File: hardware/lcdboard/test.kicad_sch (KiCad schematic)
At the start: 23 parts, among them J1 Conn_01x11_Female, J2 Conn_01x08_Shielded, J3 Conn_01x45, J4 Conn_01x11_Female, U1 AP2502

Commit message: restructure, adding branch for mux'd display board
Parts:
- added U2: 74LS157, Package_SO:TSSOP-16_4.4x5mm_P0.65mm, symbol 74xx:74LS157
- renumbered C2 to C1, C3 to C2, C4 to C3, J3 to J1, J4 to J3, J1 to J4, R11 to R1, R3 to R10, R7 to R11, R1 to R2, R2 to R3, R9 to R4, R4 to R5, R8 to R7, R10 to R8, R5 to R9, RN3 to RN1, RN4 to RN3, RN1 to RN4

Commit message: added 74CBLTV3257
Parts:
- removed RN2, RN4: 100k, Resistor_SMD:R_Array_Concave_4x0402, symbol Device:R_Pack04
- removed U2: 74LS157, Package_SO:TSSOP-16_4.4x5mm_P0.65mm, symbol 74xx:74LS157
- added RN? (x2): 100k, Resistor_SMD:R_Array_Concave_4x0402, symbol Device:R_Pack04
- added U? (x5): 74CBTLV3257, symbol 74xx:74CBTLV3257
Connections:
- net CS: no longer J4.11 (Pin_11), R8.1
- net DE: no longer J3.4 (Pin_4)
- net GND: now also RN?.5 (R4.2), RN?.6 (R3.2), RN?.7 (R2.2), RN?.8 (R1.2)
- net HSYNC: no longer J3.2 (Pin_2)
- net MISO: no longer J4.7 (Pin_7)
- net MOSI: no longer J4.8 (Pin_8)
- net PCLK: no longer J3.3 (Pin_3)
- net RS: no longer J4.10 (Pin_10)
- net SCLK: no longer J4.9 (Pin_9)
- net VSYNC: no longer J3.1 (Pin_1)
- new net: J4.11 (Pin_11), R8.1
- new net: RN?.5 (R4.2), RN?.6 (R3.2), RN?.7 (R2.2), RN?.8 (R1.2)

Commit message: schematic complete unreviewed
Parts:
- removed U? (x5): 74CBTLV3257, symbol 74xx:74CBTLV3257
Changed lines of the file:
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@@
     (pin "9")
   )
-  (symbol (lib_id "74xx:74CBTLV3257") (at 123.19 96.52 0) (unit 2)
-    (in_bom yes) (on_board yes) (fields_autoplaced)
-    (property "Reference" "U?" (id 0) (at 123.19 86.36 0))
-    (property "Value" "74CBTLV3257" (id 1) (at 123.19 88.9 0))
-    (property "Footprint" "" (id 2) (at 121.92 96.52 0)
-      (effects (font (size 1.27 1.27)) hide)
-    )
-    (property "Datasheet" "http://www.ti.com/lit/ds/symlink/sn74cbtlv3257.pdf" (id 3) (at 121.92 96.52 0)
-      (effects (font (size 1.27 1.27)) hide)
-    )
-    (pin "2")
-    (pin "3")
-    (pin "4")
-    (pin "5")
-    (pin "6")
-    (pin "7")
-    (pin "10")
-    (pin "11")
-    (pin "9")
-    (pin "12")
-    (pin "13")
-    (pin "14")
-    (pin "1")
-    (pin "15")
-    (pin "16")
-    (pin "8")
-  )
   (symbol (lib_id "power:+3V3") (at 224.79 36.83 0) (unit 1)
     (in_bom yes) (on_board yes)
@@
     )
     (pin "1")
-  )
-  (symbol (lib_id "74xx:74CBTLV3257") (at 143.51 95.25 0) (unit 3)
-    (in_bom yes) (on_board yes) (fields_autoplaced)
-    (property "Reference" "U?" (id 0) (at 143.51 85.09 0))
-    (property "Value" "74CBTLV3257" (id 1) (at 143.51 87.63 0))
-    (property "Footprint" "" (id 2) (at 142.24 95.25 0)
-      (effects (font (size 1.27 1.27)) hide)
-    )
-    (property "Datasheet" "http://www.ti.com/lit/ds/symlink/sn74cbtlv3257.pdf" (id 3) (at 142.24 95.25 0)
-      (effects (font (size 1.27 1.27)) hide)
-    )
-    (pin "2")
-    (pin "3")
-    (pin "4")
-    (pin "5")
-    (pin "6")
-    (pin "7")
-    (pin "10")
-    (pin "11")
-    (pin "9")
-    (pin "12")
-    (pin "13")
-    (pin "14")
-    (pin "1")
-    (pin "15")
-    (pin "16")
-    (pin "8")
-  )
-  (symbol (lib_id "74xx:74CBTLV3257") (at 121.92 114.3 0) (unit 4)
-    (in_bom yes) (on_board yes) (fields_autoplaced)
-    (property "Reference" "U?" (id 0) (at 121.92 104.14 0))
-    (property "Value" "74CBTLV3257" (id 1) (at 121.92 106.68 0))
-    (property "Footprint" "" (id 2) (at 120.65 114.3 0)
-      (effects (font (size 1.27 1.27)) hide)
-    )
-    (property "Datasheet" "http://www.ti.com/lit/ds/symlink/sn74cbtlv3257.pdf" (id 3) (at 120.65 114.3 0)
-      (effects (font (size 1.27 1.27)) hide)
-    )
-    (pin "2")
-    (pin "3")
-    (pin "4")
-    (pin "5")
-    (pin "6")
-    (pin "7")
-    (pin "10")
-    (pin "11")
-    (pin "9")
-    (pin "12")
-    (pin "13")
-    (pin "14")
-    (pin "1")
-    (pin "15")
-    (pin "16")
-    (pin "8")
   )
   (symbol (lib_id "power:GND") (at 147.32 133.35 0) (unit 1)
@@
     (pin "S2")
   )
-  (symbol (lib_id "74xx:74CBTLV3257") (at 156.21 109.22 0) (unit 5)
-    (in_bom yes) (on_board yes) (fields_autoplaced)
-    (property "Reference" "U?" (id 0) (at 161.29 107.9499 0)
-      (effects (font (size 1.27 1.27)) (justify left))
-    )
-    (property "Value" "74CBTLV3257" (id 1) (at 161.29 110.4899 0)
-      (effects (font (size 1.27 1.27)) (justify left))
-    )
-    (property "Footprint" "" (id 2) (at 154.94 109.22 0)
-      (effects (font (size 1.27 1.27)) hide)
-    )
-    (property "Datasheet" "http://www.ti.com/lit/ds/symlink/sn74cbtlv3257.pdf" (id 3) (at 154.94 109.22 0)
-      (effects (font (size 1.27 1.27)) hide)
-    )
-    (pin "2")
-    (pin "3")
-    (pin "4")
-    (pin "5")
-    (pin "6")
-    (pin "7")
-    (pin "10")
-    (pin "11")
-    (pin "9")
-    (pin "12")
-    (pin "13")
-    (pin "14")
-    (pin "1")
-    (pin "15")
-    (pin "16")
-    (pin "8")
-  )
   (symbol (lib_id "power:+3V3") (at 140.97 123.19 0) (unit 1)
     (in_bom yes) (on_board yes)
@@
     )
     (pin "1")
-  )
-  (symbol (lib_id "74xx:74CBTLV3257") (at 123.19 77.47 0) (unit 1)
-    (in_bom yes) (on_board yes) (fields_autoplaced)
-    (property "Reference" "U?" (id 0) (at 123.19 67.31 0))
-    (property "Value" "74CBTLV3257" (id 1) (at 123.19 69.85 0))
-    (property "Footprint" "" (id 2) (at 121.92 77.47 0)
-      (effects (font (size 1.27 1.27)) hide)
-    )
-    (property "Datasheet" "http://www.ti.com/lit/ds/symlink/sn74cbtlv3257.pdf" (id 3) (at 121.92 77.47 0)
-      (effects (font (size 1.27 1.27)) hide)
-    )
-    (pin "2")
-    (pin "3")
-    (pin "4")
-    (pin "5")
-    (pin "6")
-    (pin "7")
-    (pin "10")
-    (pin "11")
-    (pin "9")
-    (pin "12")
-    (pin "13")
-    (pin "14")
-    (pin "1")
-    (pin "15")
-    (pin "16")
-    (pin "8")
   )
   (symbol (lib_id "Device:R_Small") (at 116.84 46.99 180) (unit 1)
@@
       (reference "U1") (unit 1) (value "AP2502") (footprint "Package_TO_SOT_SMD:SOT-23-6")
     )
-    (path "/a162abfb-26f5-4e85-90d4-bb1627c202a7"
-      (reference "U?") (unit 1) (value "74CBTLV3257") (footprint "Package_SO:TSSOP-16_4.4x5mm_P0.65mm")
-    )
-    (path "/4a0105e0-6e23-41fb-90aa-e6380344c42e"
-      (reference "U?") (unit 2) (value "74CBTLV3257") (footprint "Package_SO:TSSOP-16_4.4x5mm_P0.65mm")
-    )
-    (path "/53a37b36-3e0e-4979-b4cb-948efa215072"
-      (reference "U?") (unit 3) (value "74CBTLV3257") (footprint "Package_SO:TSSOP-16_4.4x5mm_P0.65mm")
-    )
-    (path "/5a3a8ab8-1f8a-4d95-bee8-6ef02c652fa3"
-      (reference "U?") (unit 4) (value "74CBTLV3257") (footprint "Package_SO:TSSOP-16_4.4x5mm_P0.65mm")
-    )
-    (path "/906e02e9-212a-48d2-b32e-b5600a0663c8"
-      (reference "U?") (unit 5) (value "74CBTLV3257") (footprint "Package_SO:TSSOP-16_4.4x5mm_P0.65mm")
-    )
-  )
+  )

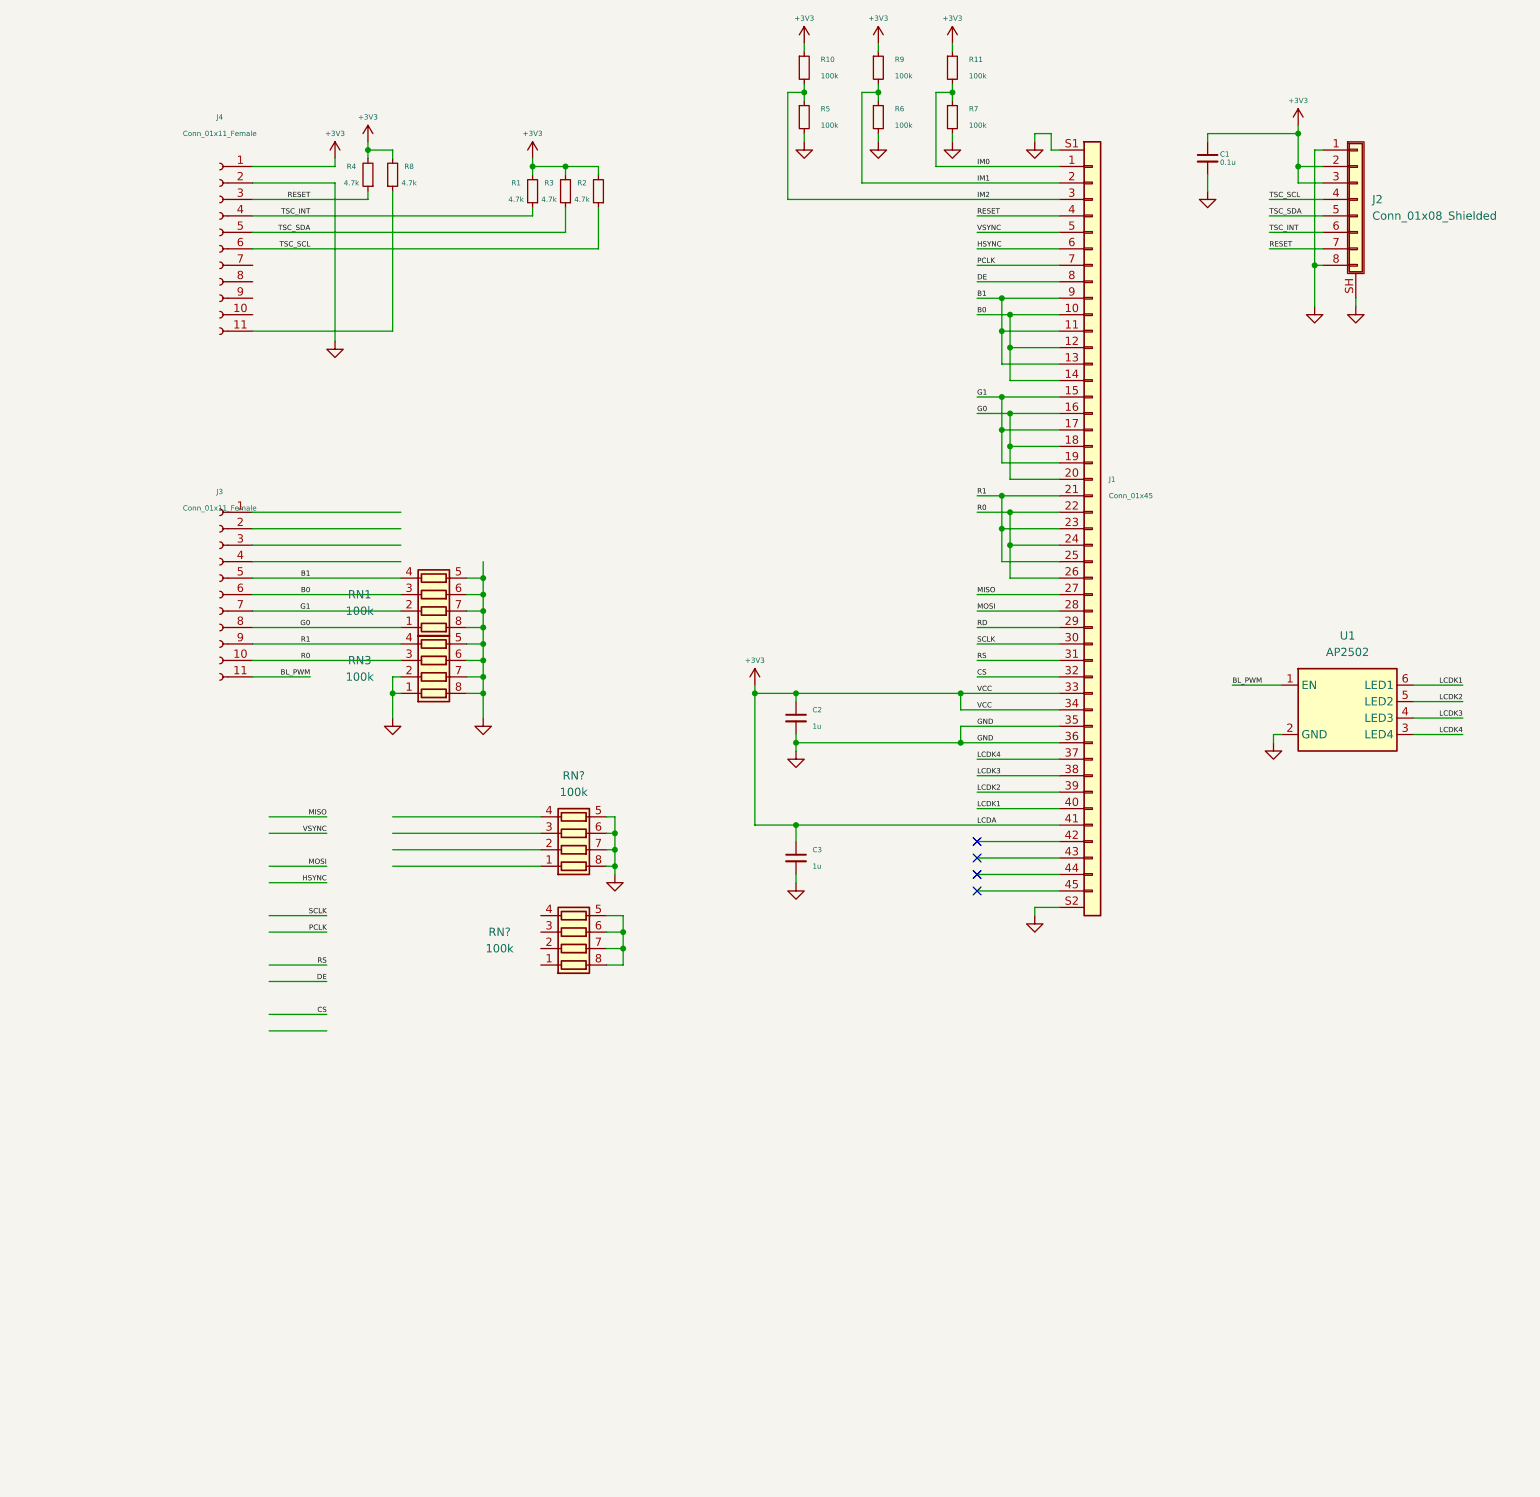
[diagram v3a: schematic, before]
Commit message: split back out condensed board into lcdboard and base
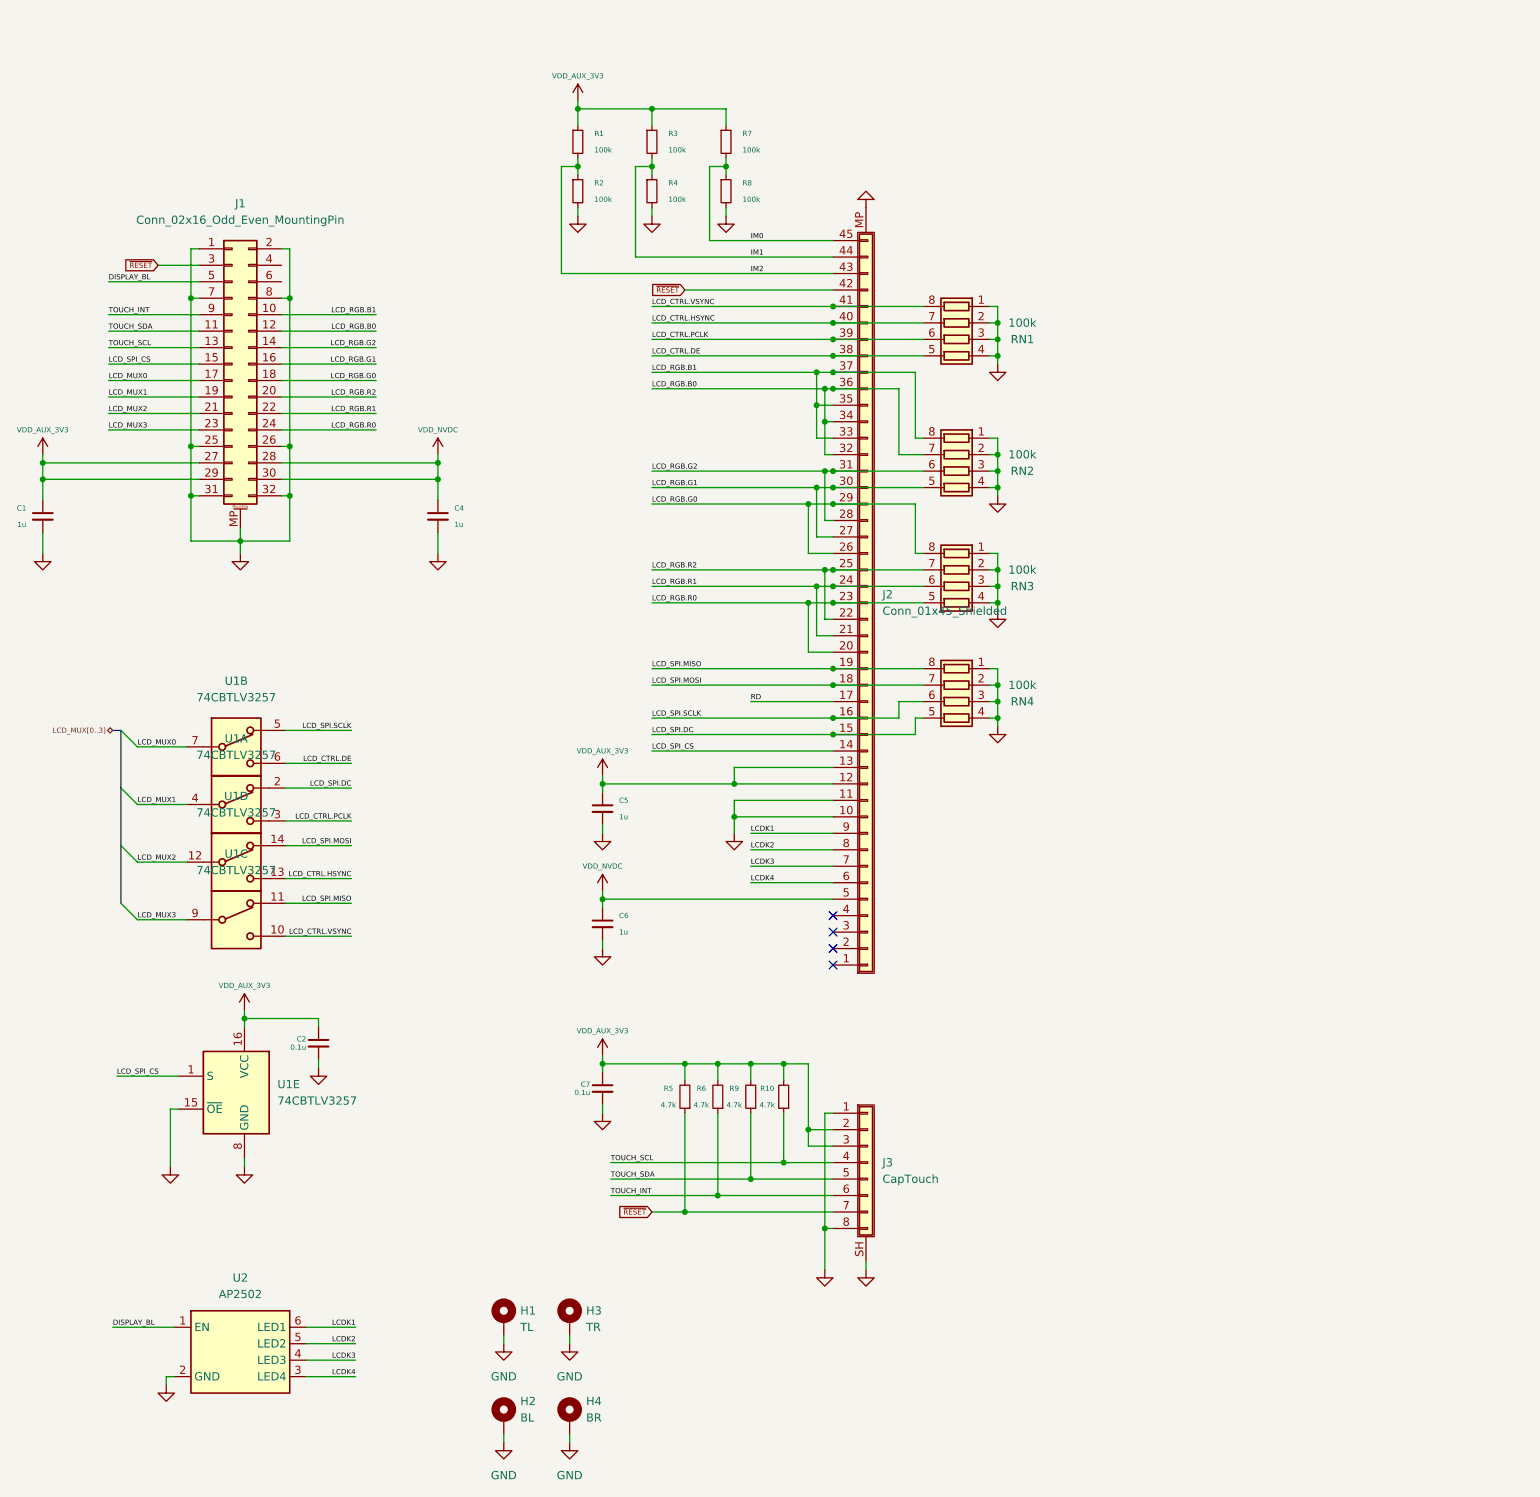
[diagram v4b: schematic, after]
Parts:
- removed C3: 1u, Capacitor_SMD:C_0603_1608Metric, symbol Device:C_Small
- removed J1: Conn_01x45, Connector_FFC-FPC:Hirose_FH12-45S-0.5SH_1x45-1MP_P0.50mm_Horizontal, symbol Connector_Generic:Conn_01x40
- removed J2: Conn_01x08_Shielded, Connector_FFC-FPC:TE_0-1734839-8_1x08-1MP_P0.5mm_Horizontal, symbol Connector_Generic_Shielded:Conn_01x08_Shielded
- removed J3, J4: Conn_01x11_Female, Connector_PinHeader_2.54mm:PinHeader_1x11_P2.54mm_Vertical, symbol Connector:Conn_01x11_Female
- removed R11: 100k, Resistor_SMD:R_0402_1005Metric, symbol Device:R_Small
- removed RN? (x2): 100k, Resistor_SMD:R_Array_Concave_4x0402, symbol Device:R_Pack04
- removed U1: AP2502, Package_TO_SOT_SMD:SOT-23-6, symbol bt_PMIC_Linear:AP2502
- added C4, C5, C6: 1u, Capacitor_SMD:C_0603_1608Metric, symbol Device:C_Small
- added C7: 0.1u, Capacitor_SMD:C_0402_1005Metric, symbol Device:C_Small
- added H1: TL, Mounting_Wuerth:Mounting_Wuerth_WA-SMSI-M1.6_H2mm_9774020633, symbol Mechanical:MountingHole_Pad
- added H2: BL, Mounting_Wuerth:Mounting_Wuerth_WA-SMSI-M1.6_H2mm_9774020633, symbol Mechanical:MountingHole_Pad
- added H3: TR, Mounting_Wuerth:Mounting_Wuerth_WA-SMSI-M1.6_H2mm_9774020633, symbol Mechanical:MountingHole_Pad
- added H4: BR, Mounting_Wuerth:Mounting_Wuerth_WA-SMSI-M1.6_H2mm_9774020633, symbol Mechanical:MountingHole_Pad
- added J1: Conn_02x16_Odd_Even_MountingPin, Connector_Molex:Molex_SlimStack_502426-3210_2x16_P0.40mm_Vertical, symbol Connector_Generic_MountingPin:Conn_02x16_Odd_Even_MountingPin
- added J2: Conn_01x45_Shielded, Connector_FFC-FPC:Hirose_FH12-45S-0.5SH_1x45-1MP_P0.50mm_Horizontal, symbol bt_Connector:Conn_01x45_Shielded
- added J3: CapTouch, Connector_FFC-FPC:TE_0-1734839-8_1x08-1MP_P0.5mm_Horizontal, symbol Connector_Generic_Shielded:Conn_01x08_Shielded
- added RN2, RN4: 100k, Resistor_SMD:R_Array_Concave_4x0402, symbol Device:R_Pack04
- added U1: 74CBTLV3257, Package_SO:TSSOP-16_4.4x5mm_P0.65mm, symbol 74xx:74CBTLV3257
- added U2: AP2502, Package_TO_SOT_SMD:SOT-23-6, symbol bt_PMIC_Linear:AP2502
- C1: value 0.1u -> 1u; footprint Capacitor_SMD:C_0402_1005Metric -> Capacitor_SMD:C_0603_1608Metric
- C2: value 1u -> 0.1u; footprint Capacitor_SMD:C_0603_1608Metric -> Capacitor_SMD:C_0402_1005Metric
- R1, R2, R3, R4, R8: value 4.7k -> 100k
- R10, R5, R6, R9: value 100k -> 4.7k
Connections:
- net B0 is gone; now on net GND: RN1.3 (R3.1)
- net B1 is gone; now on net GND: RN1.4 (R4.1)
- net G0 is gone; now on net GND: RN1.1 (R1.1)
- net G1 is gone; now on net GND: RN1.2 (R2.1)
- net R0 is gone; now on net GND: RN3.3 (R3.1)
- net R1 is gone; now on net GND: RN3.4 (R4.1)
- net RESET is gone; now on net IM1: R4.1
- net TSC_SCL is gone; now on net IM2: R2.1
- net TSC_SDA is gone; now on net VDD_AUX_3V3: R3.1
- net GND: now also R2.2, R4.2, R8.2, C4.2, C5.2, C6.2, C7.2, H1.1, H2.1, H3.1, H4.1, J1.1 (Pin_1), J1.2 (Pin_2), J1.25 (Pin_25), J1.26 (Pin_26), J1.31 (Pin_31), J1.32 (Pin_32), J1.7 (Pin_7), J1.8 (Pin_8), J1.MP (MountPin), J2.10 (Pin_10), J2.11 (Pin_11), J2.MP (Mount), J3.1 (Pin_1), J3.8 (Pin_8), J3.SH (Shield), RN2.1 (R1.1), RN2.2 (R2.1), RN2.3 (R3.1), RN2.4 (R4.1), RN4.1 (R1.1), RN4.2 (R2.1), RN4.3 (R3.1), RN4.4 (R4.1), U1.15 (~{OE}), U1.8 (GND), U2.2 (GND); no longer R5.2, R6.2, R7.2, RN1.5 (R4.2), RN1.6 (R3.2), RN1.7 (R2.2), RN1.8 (R1.2), RN3.5 (R4.2), RN3.6 (R3.2), RN3.7 (R2.2), RN3.8 (R1.2)
- net IM0: now also R7.2, R8.1, J2.45 (Pin_45); no longer R7.1
- net IM1: now also R3.2, J2.44 (Pin_44); no longer R6.1, R9.2
- net IM2: now also R1.2, J2.43 (Pin_43); no longer R10.2, R5.1
- net LCDK1: now also J2.9 (Pin_9), U2.6 (LED1)
- net LCDK2: now also J2.8 (Pin_8), U2.5 (LED2)
- net LCDK3: now also J2.7 (Pin_7), U2.4 (LED3)
- net LCDK4: now also J2.6 (Pin_6), U2.3 (LED4)
- net RD: now also J2.17 (Pin_17)
- removed net +3V3: C1.1, C2.1, R1.2, R10.1, R2.2, R3.2, R4.2, R8.2, R9.1
- net TSC_INT renamed VDD_AUX_3V3
- net VDD_AUX_3V3: now also C1.1, C2.1, R10.2, R5.2, R6.2, R7.1, R9.2, C5.1, C7.1, J1.27 (Pin_27), J1.29 (Pin_29), J2.12 (Pin_12), J2.13 (Pin_13), J3.2 (Pin_2), J3.3 (Pin_3), U1.16 (VCC)
- new net DISPLAY_BL: J1.5 (Pin_5), U2.1 (EN)
- new net LCD_CTRL.DE: J2.38 (Pin_38), RN1.5 (R4.2), U1.6
- new net LCD_CTRL.HSYNC: J2.40 (Pin_40), RN1.7 (R2.2), U1.13
- new net LCD_CTRL.PCLK: J2.39 (Pin_39), RN1.6 (R3.2), U1.3
- new net LCD_CTRL.VSYNC: J2.41 (Pin_41), RN1.8 (R1.2), U1.10
- new net LCD_MUX0: J1.17 (Pin_17), U1.7
- new net LCD_MUX1: J1.19 (Pin_19), U1.4
- new net LCD_MUX2: J1.21 (Pin_21), U1.12
- new net LCD_MUX3: J1.23 (Pin_23), U1.9
- new net LCD_RGB.B0: J1.12 (Pin_12), J2.32 (Pin_32), J2.34 (Pin_34), J2.36 (Pin_36), RN2.7 (R2.2)
- new net LCD_RGB.B1: J1.10 (Pin_10), J2.33 (Pin_33), J2.35 (Pin_35), J2.37 (Pin_37), RN2.8 (R1.2)
- new net LCD_RGB.G0: J1.18 (Pin_18), J2.26 (Pin_26), J2.29 (Pin_29), RN3.8 (R1.2)
- new net LCD_RGB.G1: J1.16 (Pin_16), J2.27 (Pin_27), J2.30 (Pin_30), RN2.5 (R4.2)
- new net LCD_RGB.G2: J1.14 (Pin_14), J2.28 (Pin_28), J2.31 (Pin_31), RN2.6 (R3.2)
- new net LCD_RGB.R0: J1.24 (Pin_24), J2.20 (Pin_20), J2.23 (Pin_23), RN3.5 (R4.2)
- new net LCD_RGB.R1: J1.22 (Pin_22), J2.21 (Pin_21), J2.24 (Pin_24), RN3.6 (R3.2)
- new net LCD_RGB.R2: J1.20 (Pin_20), J2.22 (Pin_22), J2.25 (Pin_25), RN3.7 (R2.2)
- new net LCD_SPI.DC: J2.15 (Pin_15), RN4.5 (R4.2), U1.2
- new net LCD_SPI.MISO: J2.19 (Pin_19), RN4.8 (R1.2), U1.11
- new net LCD_SPI.MOSI: J2.18 (Pin_18), RN4.7 (R2.2), U1.14
- new net LCD_SPI.SCLK: J2.16 (Pin_16), RN4.6 (R3.2), U1.5
- new net LCD_SPI_CS: J1.15 (Pin_15), J2.14 (Pin_14), U1.1 (S)
- new net TOUCH_INT: J1.9 (Pin_9), J3.6 (Pin_6), R6.1
- new net TOUCH_SCL: J1.13 (Pin_13), J3.4 (Pin_4), R10.1
- new net TOUCH_SDA: J1.11 (Pin_11), J3.5 (Pin_5), R9.1
- new net VDD_NVDC: C4.1, C6.1, J1.28 (Pin_28), J1.30 (Pin_30), J2.5 (Pin_5)
- new net ~{RESET}: J1.3 (Pin_3), J2.42 (Pin_42), J3.7 (Pin_7), R5.1
